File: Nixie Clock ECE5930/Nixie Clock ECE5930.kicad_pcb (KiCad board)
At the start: 2 copper layers, 192 x 43.5 mm, 37 parts, among them J1 Conn_02x03_Top_Bottom, J2 USB_C_Receptacle_PowerOnly_6P, J3 Conn_01x03, SW1 SW_Push, SW2 SW_Push, SW3 SW_Push, U1 ATmega328P-P, U2 HV5622, U3 HV5622, U4 L78L05_SO8, U5 DS3231N, Y1 Crystal

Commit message: rewire
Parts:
- R1, R2, R3, U4, Y1: moved to B.Cu
- moved C5 169.1 mm to (58.5, 27.0), turned to 0 degrees
- moved C4 162.1 mm to (58.5, 36.0), turned to 0 degrees
- moved U4 160.7 mm to (87.0, 52.7), turned to 0 degrees
- moved C1 159.5 mm to (58.5, 61.5), turned to 0 degrees
- moved J2 147.6 mm to (87.0, 62.2)
- moved J3 146.6 mm to (96.0, 54.6)
- moved BT1 126.5 mm to (113.7, 33.7), turned to 180 degrees
- moved R2 118.2 mm to (64.0, 36.0), turned to 0 degrees
- moved R3 118.1 mm to (64.0, 31.0)
- moved C3 114.0 mm to (58.5, 53.0), turned to 0 degrees
- moved U5 105.0 mm to (82.5, 40.6)
- moved C2 104.3 mm to (58.5, 45.0)
- moved Y1 103.8 mm to (63.8, 49.0), turned to 90 degrees
- moved U1 96.2 mm to (66.5, 25.8), turned to 0 degrees
- moved R1 92.9 mm to (64.0, 27.0)
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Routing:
- net Net-(U1-PD4): track 79.7 -> 188.2 mm, vias 3 -> 6
- net Net-(U1-PD3): track 84.5 -> 181.7 mm, vias 6 -> 5
- net Net-(U1-PD2): track 85.8 -> 180.1 mm, vias 5 -> 4
- net HT: track 14.8 -> 105.3 mm
- net Net-(U1-PD1): track 87.9 -> 177.3 mm, vias 4 -> 9
- net Net-(U1-PD0): track 0.00 -> 86.7 mm, vias 0 -> 1
- net +5V: track 373.9 -> 444.0 mm, vias 7 -> 9
- net Net-(U5-Vbat): track 94.9 -> 39.0 mm, vias 1 -> 0
- net Net-(U2-HV12): track 25.3 -> 55.5 mm, vias 0 -> 1
- net Net-(U2-HV30): track 56.0 -> 27.8 mm, vias 2 -> 0
- net Net-(U3-HV27): track 50.1 -> 23.5 mm
- net Net-(U1-PC5): track 2.18 -> 28.3 mm, vias 1 -> 2
- net Net-(U3-HV28): track 50.7 -> 24.6 mm
- net Net-(U3-HV26): track 49.9 -> 23.9 mm
- net Net-(U3-HV21): track 74.3 -> 48.4 mm, vias 1 -> 0
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
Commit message: added button STEP
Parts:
- removed SW1, SW2, SW3: SW_Push, Button_Switch_SMD:Nidec_Copal_CAS-120A
- added SW4: 2-1825910-7, footprints:SW4_1825910-G_TEC, F.Cu at (84.0, 32.0)
- added SW5: 2-1825910-7, footprints:SW4_1825910-G_TEC, F.Cu at (94.0, 32.0)
- added SW6: 2-1825910-7, footprints:SW4_1825910-G_TEC, F.Cu at (104.0, 32.0)
- moved BT1 11.7 mm to (125.3, 35.0)
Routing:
- net +5V: track 444.0 -> 325.3 mm, vias 9 -> 7
- net Net-(U1-PD7): track 42.3 -> 0.00 mm
- net Net-(U5-Vbat): track 39.0 -> 0.00 mm
- net Net-(U1-PD5): track 31.2 -> 0.00 mm
- net Net-(U1-PD6): track 28.7 -> 0.00 mm

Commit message: added button STEP
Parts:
- removed SW4, SW5, SW6: 2-1825910-7, footprints:SW4_1825910-G_TEC
- added SW1: SW_Push, Button_Switch_SMD:Nidec_Copal_CAS-120A, F.Cu at (88.8, 30.8)
- added SW2: SW_Push, Button_Switch_SMD:Nidec_Copal_CAS-120A, F.Cu at (78.8, 30.8)
- added SW3: SW_Push, Button_Switch_SMD:Nidec_Copal_CAS-120A, F.Cu at (83.8, 30.8)
- moved BT1 11.7 mm to (113.7, 33.7)
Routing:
- net +5V: track 325.3 -> 444.0 mm, vias 7 -> 9
- net Net-(U1-PD7): track 0.00 -> 42.3 mm
- net Net-(U5-Vbat): track 0.00 -> 39.0 mm
- net Net-(U1-PD5): track 0.00 -> 31.2 mm
- net Net-(U1-PD6): track 0.00 -> 28.7 mm

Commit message: holy shit im gonna die
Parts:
- removed J2: USB_C_Receptacle_PowerOnly_6P, Connector_USB:USB_C_Plug_JAE_DX07P024AJ1
- removed SW1, SW2, SW3: SW_Push, Button_Switch_SMD:Nidec_Copal_CAS-120A
- added REF**: MountingHole_2.1mm, MountingHole:MountingHole_2.1mm, F.Cu at (241.9, 26.7)
- added REF**: MountingHole_2.1mm, MountingHole:MountingHole_2.1mm, F.Cu at (33.0, 26.7)
- added REF**: MountingHole_2.1mm, MountingHole:MountingHole_2.1mm, F.Cu at (33.0, 61.6)
- added REF**: MountingHole_2.1mm, MountingHole:MountingHole_2.1mm, F.Cu at (241.9, 61.6)
- added REF**: CUI_PJ-002B, PJ_002B:CUI_PJ-002B, B.Cu at (85.7, 52.0)
- added SW4: 2-1825910-7, footprints:SW4_1825910-G_TEC, F.Cu at (84.2, 33.5)
- added SW5: 2-1825910-7, footprints:SW4_1825910-G_TEC, F.Cu at (92.8, 33.5)
- added SW6: 2-1825910-7, footprints:SW4_1825910-G_TEC, F.Cu at (101.4, 33.5)
- moved BT1 72.4 mm to (41.3, 34.1), turned to -90 degrees
- moved U4 7.75 mm to (93.3, 48.3)
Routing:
- net Net-(U1-PD5): track 31.2 -> 70.7 mm
- net +5V: track 444.0 -> 407.8 mm, vias 9 -> 10
- net (no net): track 0.00 -> 32.6 mm
- net +12V: track 27.6 -> 4.52 mm
- net Net-(U5-Vbat): track 39.0 -> 50.7 mm, vias 0 -> 3
- net Net-(U1-PD6): track 28.7 -> 37.3 mm, vias 0 -> 1
- net Net-(U1-PC4): track 25.1 -> 26.4 mm
- net Net-(U1-PD7): track 42.3 -> 41.7 mm, vias 0 -> 2
- net HT: track 105.3 -> 105.8 mm
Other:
- board size 192 x 43.5 mm -> 217.4 x 43.5 mm
- board text added: "Bobby Thompson REV: 1.0-A"

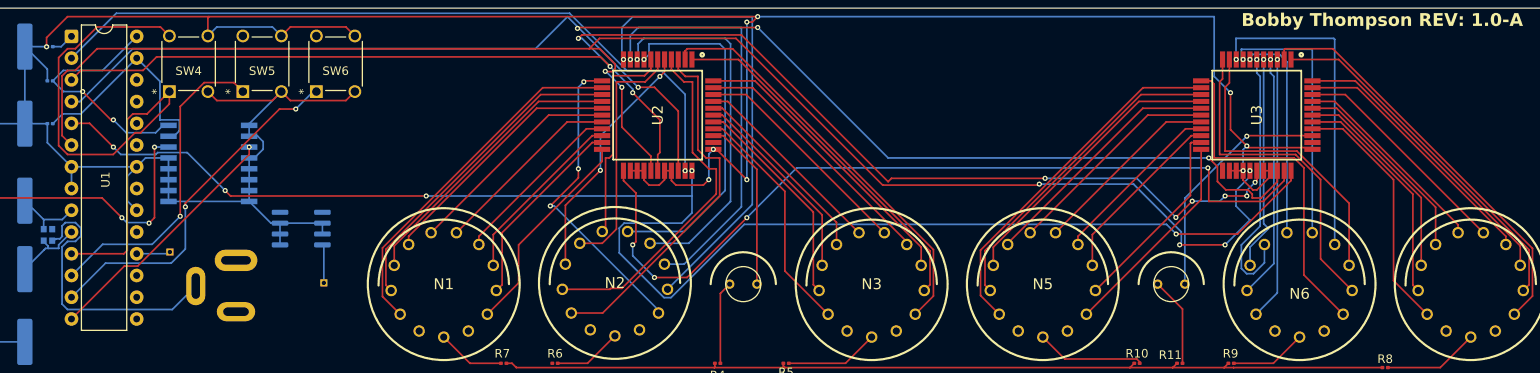
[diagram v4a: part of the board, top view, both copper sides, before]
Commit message: 3d models yum
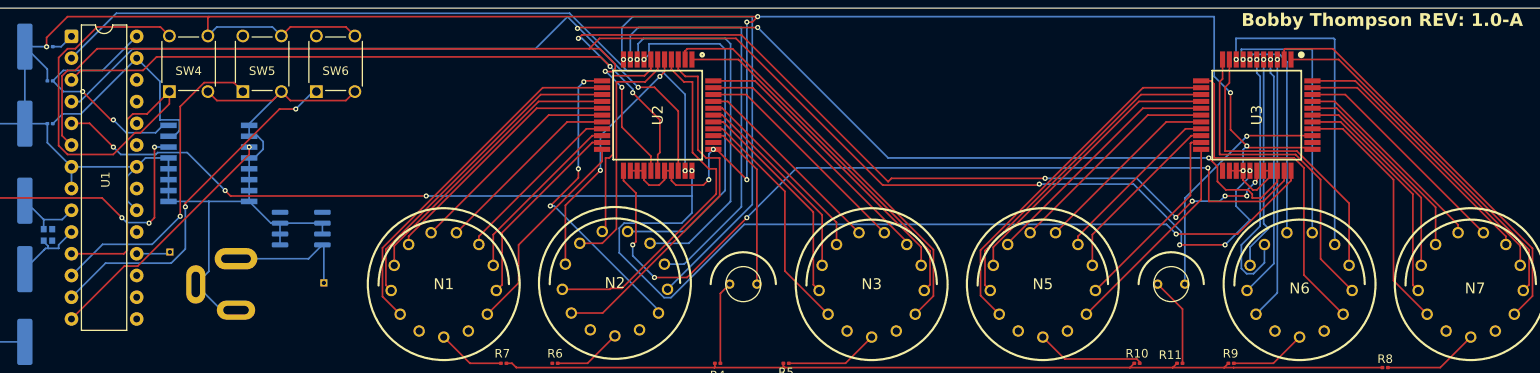
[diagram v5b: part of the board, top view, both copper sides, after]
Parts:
- removed the REF** at (85.7, 52.0)
- added J2: PJ-002B, PJ_002B:CUI_PJ-002B, B.Cu at (85.7, 51.8)
- U3: footprint HV5622PG-G:QFP80P1390X1390X235-44N -> KiCad:QFP80P1390X1390X235-44N
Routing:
- net (no net): track 32.6 -> 0.00 mm
- net +5V: track 407.8 -> 424.1 mm
- net +12V: track 4.52 -> 15.3 mm

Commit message: final commit i hope
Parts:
- removed Y1: Crystal, nixiemisc:nixiemisc-CRYSTAL-SMD-2.0X1.6MM
- added C4: C, Capacitor_SMD:C_2220_5750Metric, F.Cu at (103.3, 39.2)
- added C5: C, Capacitor_SMD:C_2220_5750Metric, F.Cu at (94.2, 39.2)
- added C6: ABS07-32.768KHZ-T, ABS07_32_768KHZ_T (1):CAP_ABS07-32.768KHZ-T_ABR, F.Cu at (63.5, 48.9)
- added U6: L78L05_SOT89, Package_TO_SOT_SMD:SOT-89-3, B.Cu at (96.9, 61.0)
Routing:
- net +5V: track 424.1 -> 474.9 mm, vias 10 -> 11
- net Net-(U1-PD5): track 70.7 -> 34.8 mm
- net +12V: track 15.3 -> 27.7 mm
- net Net-(U1-PD7): track 41.7 -> 48.2 mm
- net Net-(U1-PD6): track 37.3 -> 43.8 mm
- net Net-(U1-PD2): track 180.0 -> 183.1 mm, vias 4 -> 6
- net Net-(U1-XTAL2/PB7): track 8.61 -> 11.2 mm, vias 0 -> 1
- net Net-(U1-XTAL1/PB6): track 7.94 -> 9.43 mm
- net HT: track 105.8 -> 106.3 mm
